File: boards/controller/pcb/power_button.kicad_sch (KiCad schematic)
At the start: 8 parts, among them Q201 BSS138

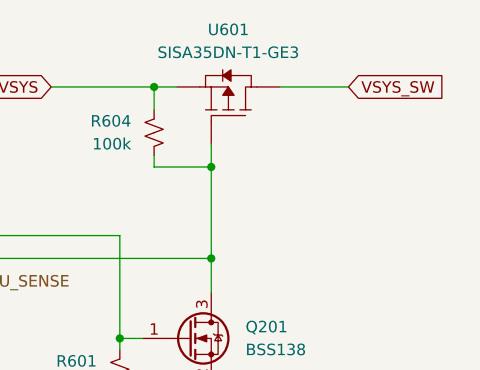
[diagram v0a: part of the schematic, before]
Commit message: controller: pcb: Update schematic
Signed-off-by: Nicholas Loehrke <nicholasnloehrke@gmail.com>
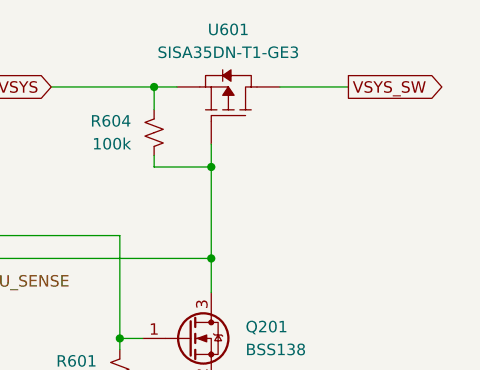
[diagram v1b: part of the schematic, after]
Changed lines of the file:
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@@
 	)
 	(global_label "VSYS_SW"
-		(shape input)
+		(shape output)
 		(at 186.69 83.82 0)
 		(fields_autoplaced yes)

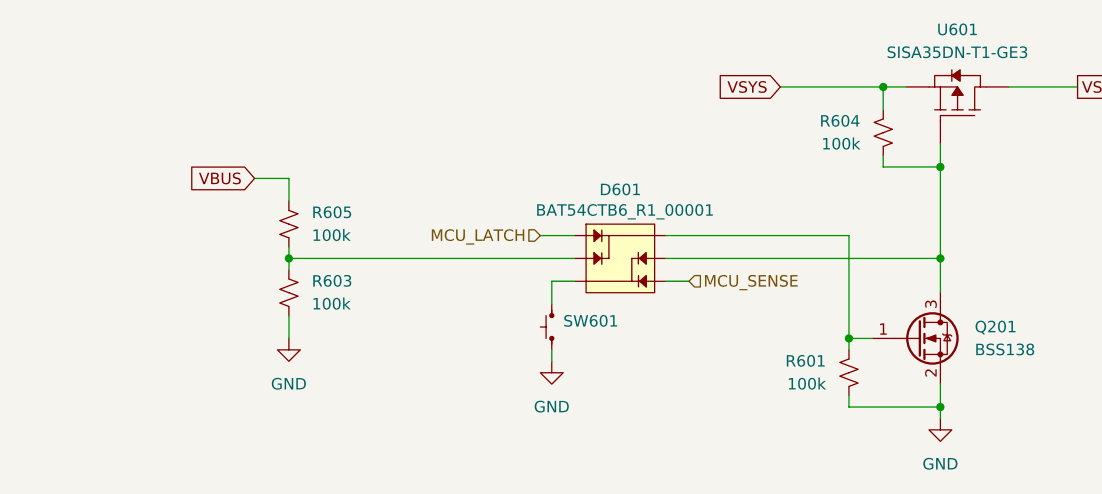
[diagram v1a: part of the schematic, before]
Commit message: controller: pcb: Update schematic
Signed-off-by: Nicholas Loehrke <nicholasnloehrke@gmail.com>
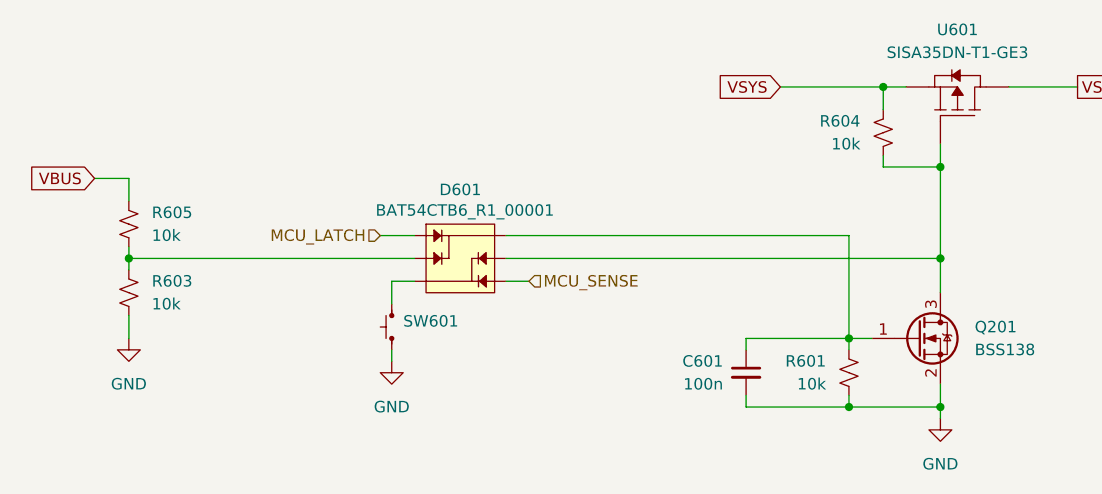
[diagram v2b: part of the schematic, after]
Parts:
- added C601: 100n, symbol Device:C_Small
- R601, R603, R604, R605: value 100k -> 10k
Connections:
- net GND: now also C601.2
- net at D601.6, Q201.1 (G), R601.1: now also C601.1
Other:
- moved on the sheet: D601, R603, R605, SW601

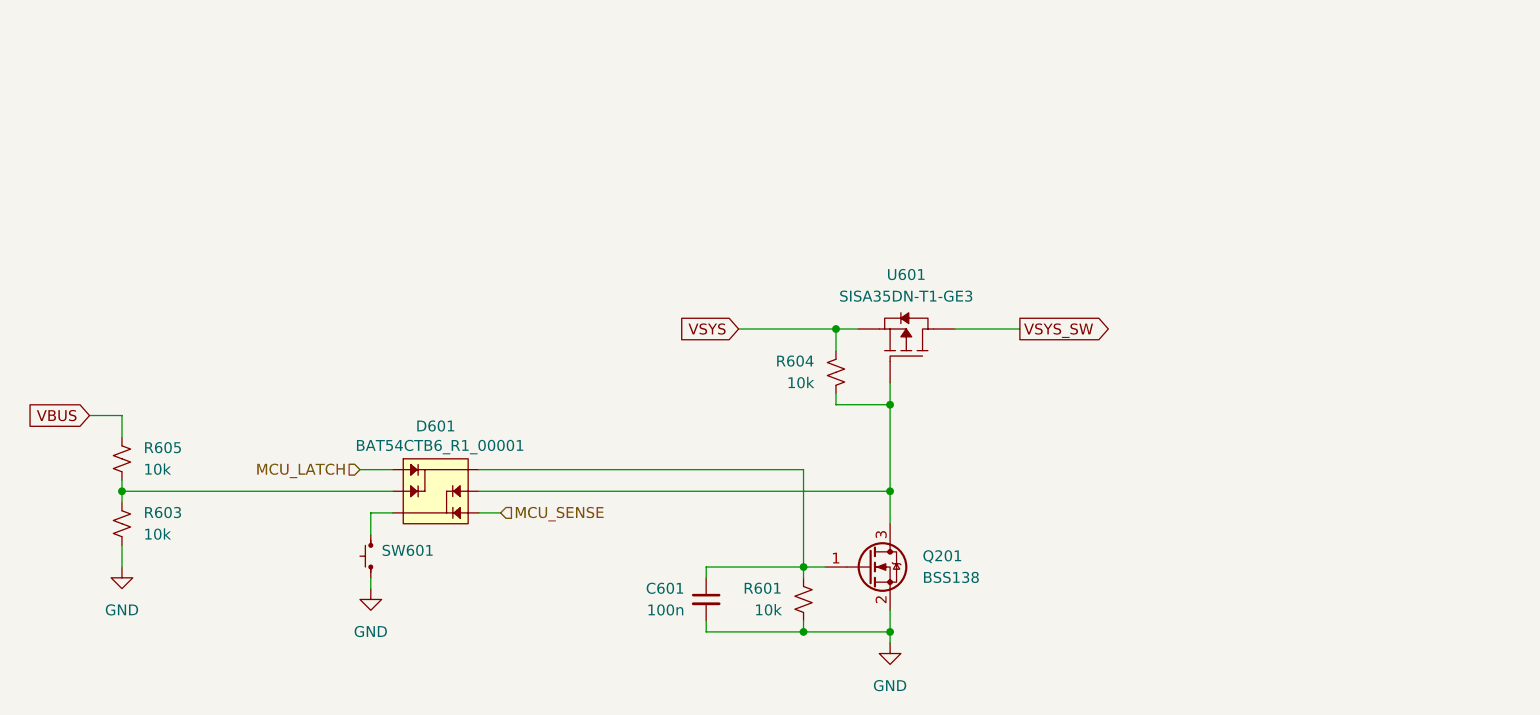
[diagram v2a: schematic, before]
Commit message: controller: pcb: Update schematic
Signed-off-by: Nicholas Loehrke <nicholasnloehrke@gmail.com>
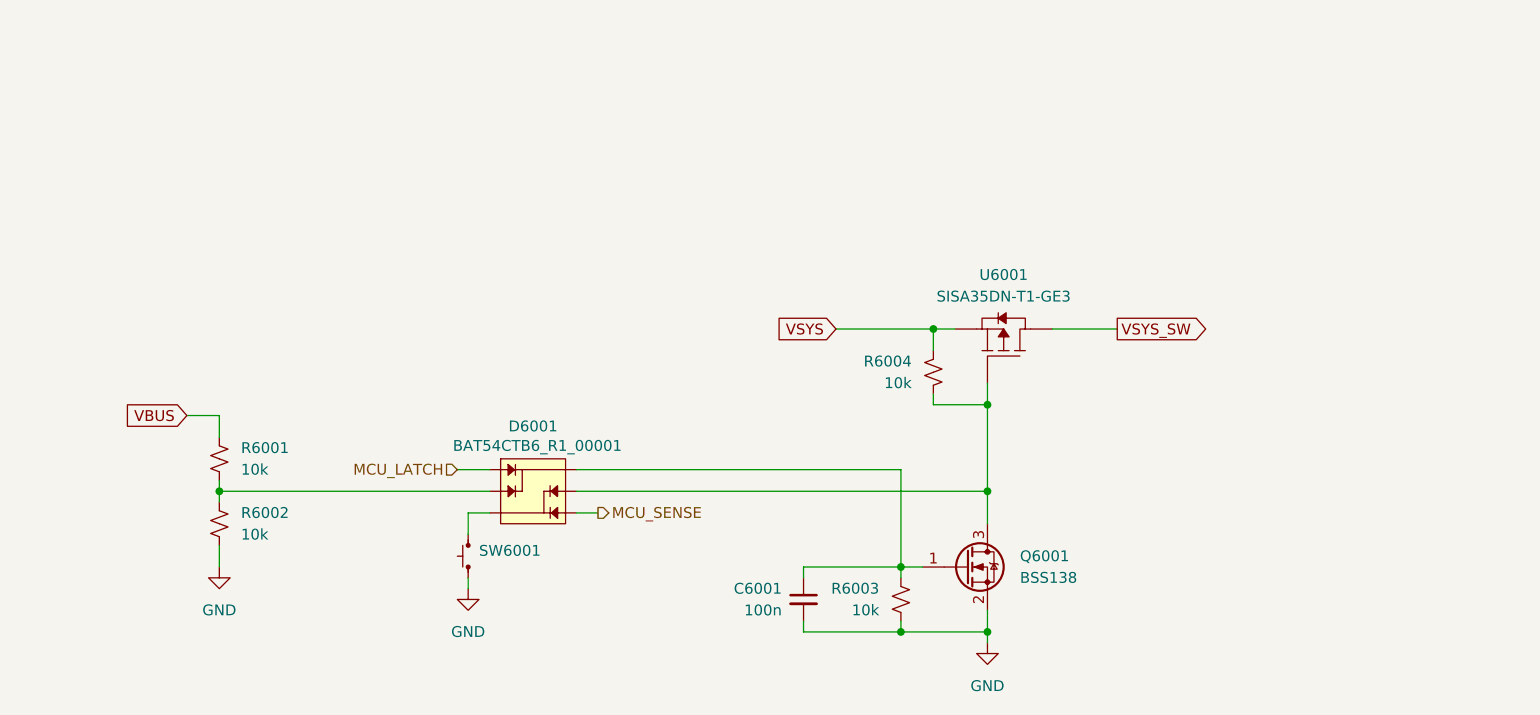
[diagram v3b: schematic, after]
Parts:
- renumbered C601 to C6001, D601 to D6001, Q201 to Q6001, R605 to R6001, R603 to R6002, R601 to R6003, R604 to R6004, SW601 to SW6001, U601 to U6001
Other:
- moved on the sheet: C6001, D6001, Q6001, R6001, R6002, R6003, R6004, SW6001, U6001

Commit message: controller: pcb: Update schematic
- Add power button pmos gate voltage clamp
- Add TVS diodes on encoders

Signed-off-by: Nicholas Loehrke <nicholasnloehrke@gmail.com>
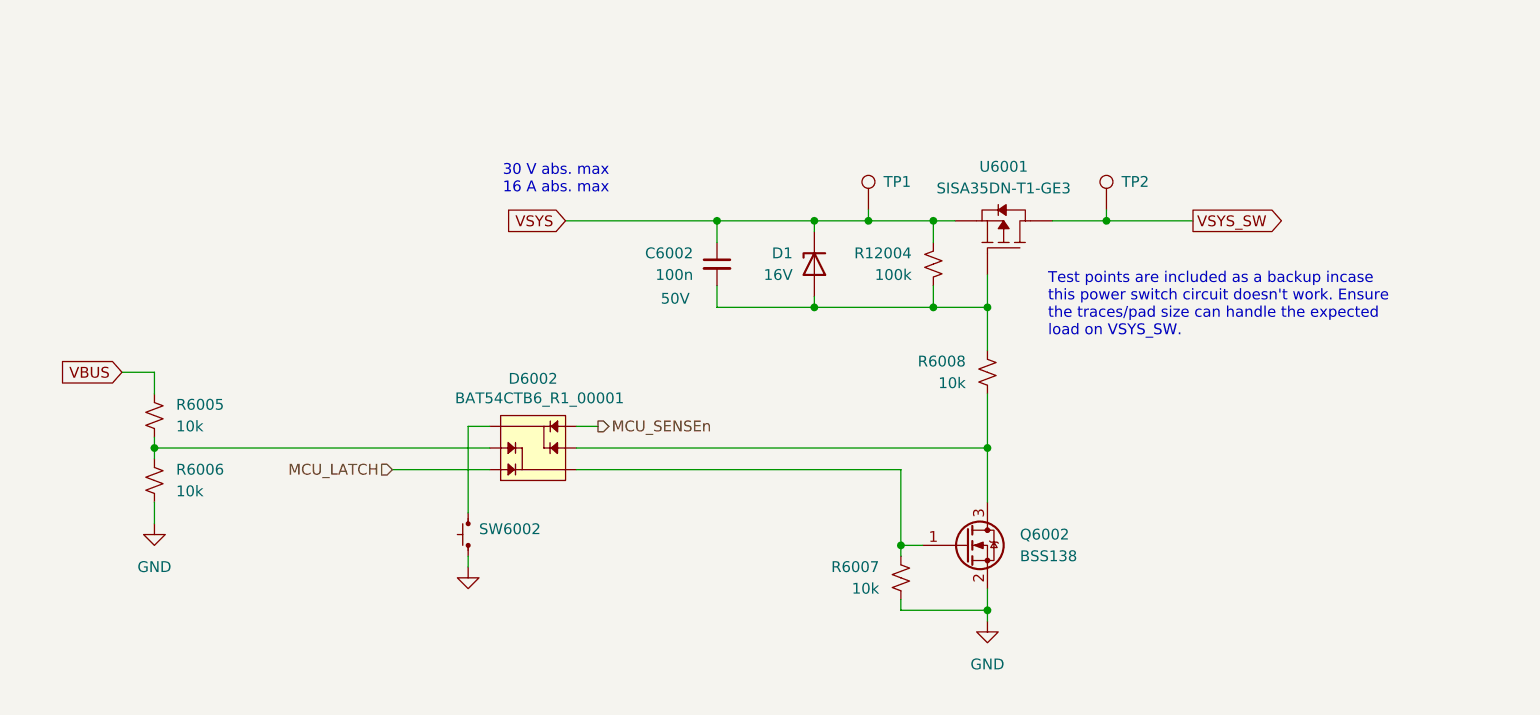
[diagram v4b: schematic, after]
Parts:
- removed C6001: 100n, symbol Device:C_Small
- removed D6001: ~, symbol BAT54CTB6_R1_00001:BAT54CTB6_R1_00001
- removed Q6001: BSS138, Package_TO_SOT_SMD:SOT-23, symbol Transistor_FET:BSS138
- removed R6001, R6002, R6003, R6004: 10k, symbol Device:R_Small_US
- removed SW6001: ~, symbol ESE-20D443:ESE-20D443
- added C6002: 100n, symbol Device:C_Small
- added D1: 16V, symbol Device:D_Zener
- added D6002: ~, symbol BAT54CTB6_R1_00001:BAT54CTB6_R1_00001
- added Q6002: BSS138, Package_TO_SOT_SMD:SOT-23, symbol Transistor_FET:BSS138
- added R12004: 100k, symbol Device:R_Small_US
- added R6005, R6006, R6007, R6008: 10k, symbol Device:R_Small_US
- added SW6002: ~, symbol ESE-20D443:ESE-20D443
- added TP1, TP2: TestPoint, symbol Connector:TestPoint
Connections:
- net GND: now also Q6002.2 (S), R6006.2, R6007.2, SW6002.1 (a), SW6002.2 (b)
- net MCU_LATCH: now also D6002.1
- net VBUS: now also R6005.1
- net VSYS: now also C6002.1, D1.1 (K), R12004.1, TP1.1
- net VSYS_SW: now also TP2.1
- net at U6001.4: now also C6002.2, D1.2 (A), R12004.2, R6008.1
- new net: D6002.3, SW6002.3 (c), SW6002.4 (d)
- new net: D6002.6, Q6002.1 (G), R6007.1
- new net: D6002.5, Q6002.3 (D), R6008.2
- new net: D6002.2, R6005.2, R6006.1
- new net MCU_SENSEn: D6002.4
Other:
- note added: "30 V abs. max 16 A abs. max"
- note added: "Test points are included as a backup incase this power switch circuit doesn't work. Ensure the traces/pad size can handle the expected load on VSYS_SW."
- moved on the sheet: U6001

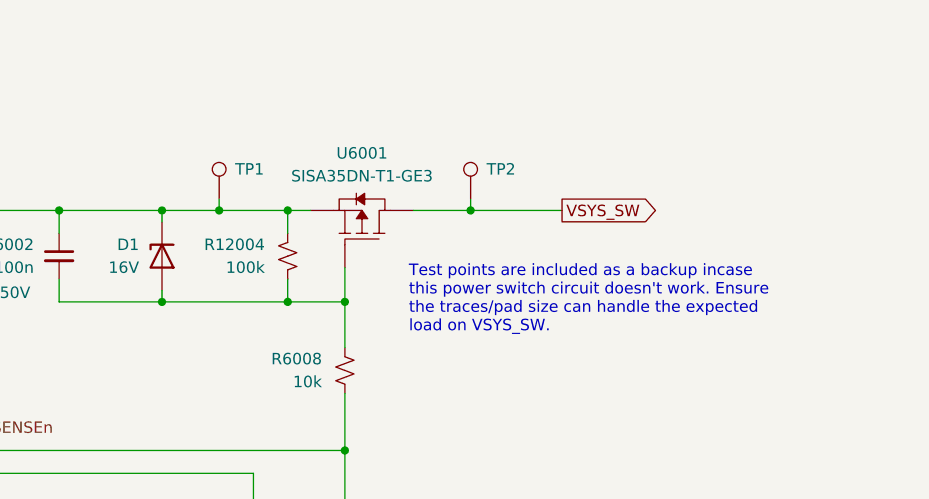
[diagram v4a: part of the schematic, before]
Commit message: controller: pcb: Update schematic
Signed-off-by: Nicholas Loehrke <nicholasnloehrke@gmail.com>
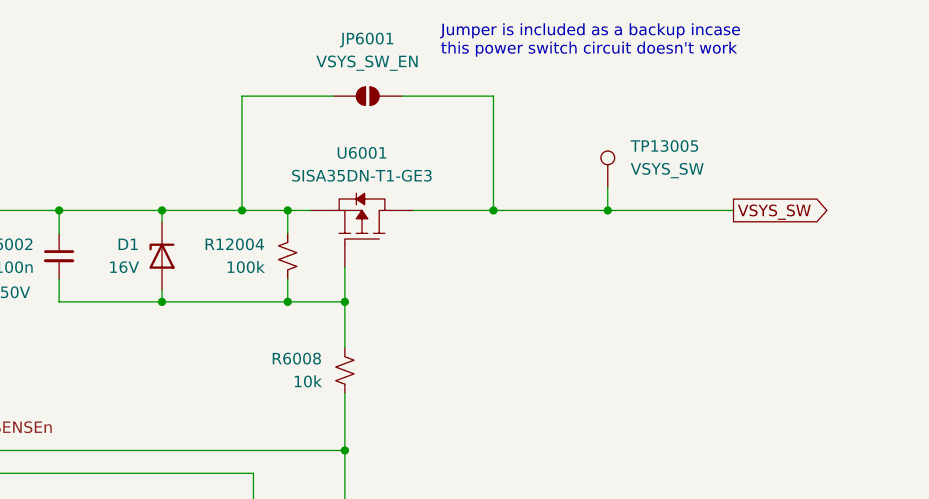
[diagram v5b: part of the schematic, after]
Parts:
- removed TP1, TP2: TestPoint, symbol Connector:TestPoint
- added JP6001: VSYS_SW_EN, symbol Jumper:SolderJumper_2_Open
- added TP13005: VSYS_SW, symbol Connector:TestPoint
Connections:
- net VSYS: now also JP6001.1 (A)
- net VSYS_SW: now also JP6001.2 (B), TP13005.1
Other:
- note added: "Jumper is included as a backup incase this power switch circuit doesn't work"
- note removed: "Test points are included as a backup incase this power switch circuit doesn't work. Ensure the traces/pad size can handle the expected load on VSYS_SW."

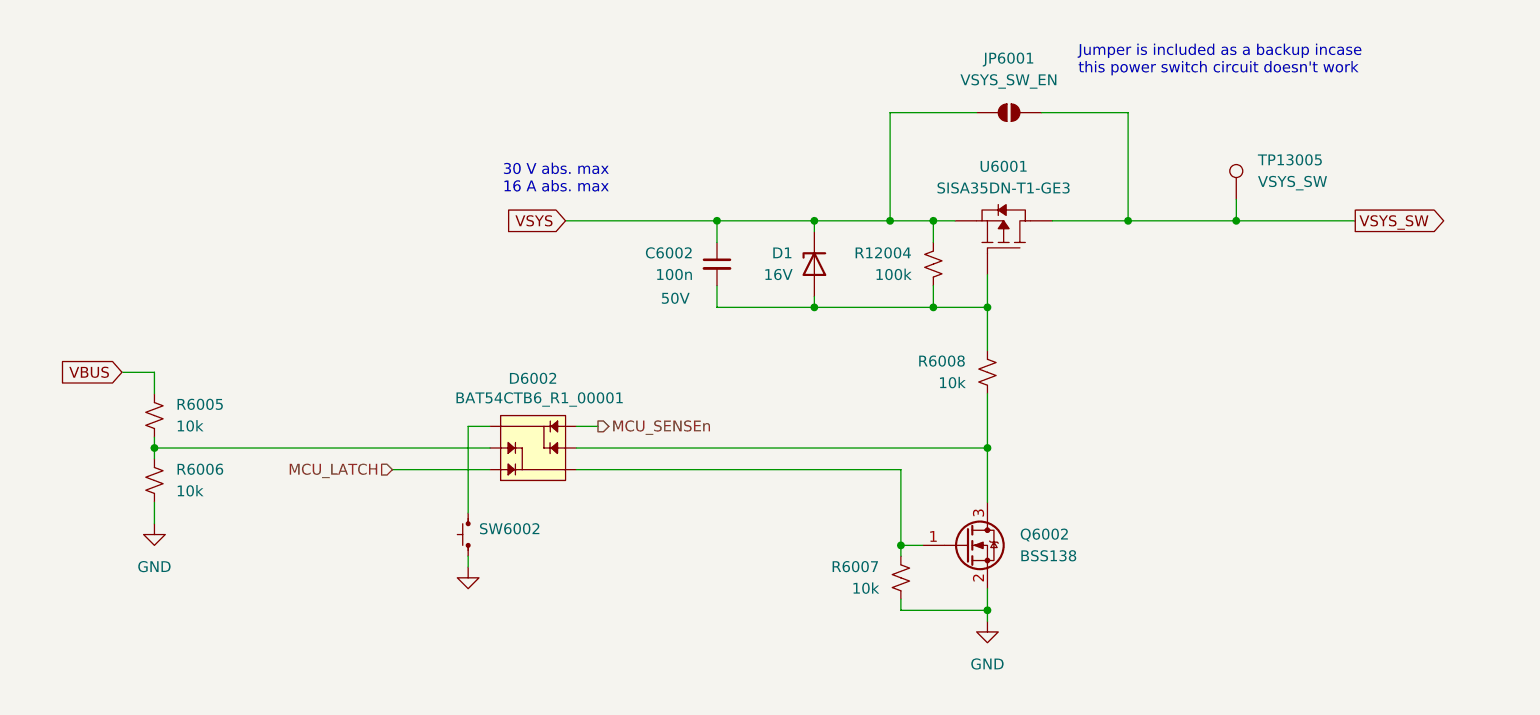
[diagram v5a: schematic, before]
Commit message: controller: pcb: Update schematic + layout
Signed-off-by: Nicholas Loehrke <nicholasnloehrke@gmail.com>
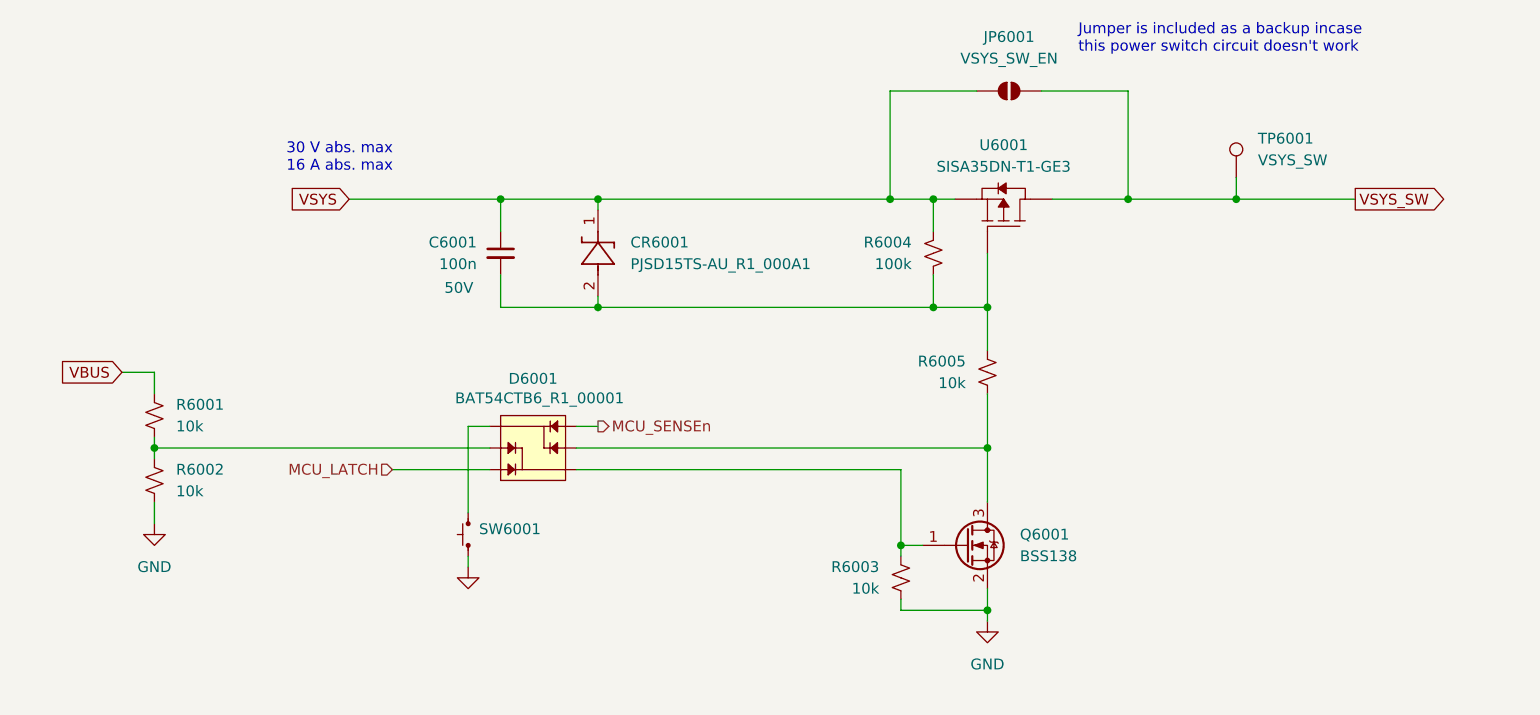
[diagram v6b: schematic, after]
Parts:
- removed D1: 16V, symbol Device:D_Zener
- added CR6001: PJSD15TS-AU_R1_000A1, PJSD15TS-AU_R1_000A1:PJSD15TS-AU_R1_000A1, symbol PJSD15TS-AU_R1_000A1:PJSD15TS-AU_R1_000A1
- C6001: renamed from C6002; footprint (none) -> Capacitor_SMD:C_0402_1005Metric
- D6001: renamed from D6002; footprint (none) -> Package_TO_SOT_SMD:SOT-563
- JP6001: footprint (none) -> Jumper:SolderJumper-2_P1.3mm_Open_RoundedPad1.0x1.5mm
- R6001: renamed from R6005; footprint (none) -> Resistor_SMD:R_0402_1005Metric
- R6002: renamed from R6006; footprint (none) -> Resistor_SMD:R_0402_1005Metric
- R6003: renamed from R6007; footprint (none) -> Resistor_SMD:R_0402_1005Metric
- R6004: renamed from R12004; footprint (none) -> Resistor_SMD:R_0402_1005Metric
- R6005: renamed from R6008; footprint (none) -> Resistor_SMD:R_0402_1005Metric
- SW6001: renamed from SW6002; footprint (none) -> ESE-20D443:ESE-20D443
- TP6001: renamed from TP13005; footprint (none) -> TestPoint:TestPoint_Pad_D1.0mm
- U6001: footprint (none) -> SISA35DN-T1-GE3:SISA35DN-T1-GE3
- renumbered Q6002 to Q6001
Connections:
- net VSYS: now also CR6001.1
- net at C6001.2, R6004.2, R6005.1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: now also CR6001.2
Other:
- moved on the sheet: C6001, JP6001, R6004, TP6001, U6001
